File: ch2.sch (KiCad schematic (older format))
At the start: 0 parts

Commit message: ch1 and ch2 are complete
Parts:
- added C10, C9: 680p, symbol Device:C_Small
- added C11, C12: 47p, symbol Device:C_Small
- added C7, C8: 100p, symbol Device:C_Small
- added J2: CH2, symbol Connector:XLR3_Ground
- added Q201, Q211: BC856BDW1, Package_TO_SOT_SMD:SOT-363_SC-70-6, symbol Transistor_BJT:BC856BDW1
- added Q202, Q212: LS844, SOT95P280X145-6N, symbol LS844-SOT-23-6L-CT:LS844-SOT-23-6L-CT
- added Q203, Q213: BC846BDW1, Package_TO_SOT_SMD:SOT-363_SC-70-6, symbol Transistor_BJT:BC846BDW1
- added Q204, Q214: BC856, Package_TO_SOT_SMD:SOT-23, symbol Transistor_BJT:BC856
- added Q205, Q215: BCP53, Package_TO_SOT_SMD:SOT-223-3_TabPin2, symbol Transistor_BJT:BCP53
- added Q206, Q216: BC846, Package_TO_SOT_SMD:SOT-23, symbol Transistor_BJT:BC846
- added Q207, Q217: BCP56, Package_TO_SOT_SMD:SOT-223-3_TabPin2, symbol Transistor_BJT:BCP56
- added R28, R29, R33, R34, R35, R36, R43, R44, R45, R46, R53, R54: 100R, symbol Device:R_Small
- added R30: 2M2, symbol Device:R_Small
- added R31, R32: 47K, symbol Device:R_Small
- added R37, R38, R47, R48: 5K6, symbol Device:R_Small
- added R39, R40, R49, R50: 470R, symbol Device:R_Small
- added R41, R42: 330R, symbol Device:R_Small
- added R51, R52: 22R, symbol Device:R_Small
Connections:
- new net: J2.2, R28.2
- new net: J2.3, R29.2
- new net: R30.1, R31.1, R32.2
- new net: C11.2, Q201.1 (E1), Q202.2 (D1), Q204.1 (B), R39.2
- new net: Q202.3 (S1), R34.2
- new net: C11.1, Q202.4 (G2), Q205.2 (C), Q205.4 (C), Q207.2 (C), Q207.4 (C), R53.2
- new net: C9.1, Q201.2 (B1), Q201.4 (E2), Q201.5 (B2), Q202.5 (D2)
- new net: Q202.6 (S2), R44.2
- new net: C9.2, R39.1
- new net: Q201.6 (C1), R33.1
- new net: Q201.3 (C2), R43.1
- new net: Q203.6 (C1), R34.1, R44.1
- new net: Q203.2 (B1), Q203.3 (C2), R37.1
- new net: Q203.1 (E1), Q203.5 (B2), R41.2
- new net: Q204.2 (E), Q205.1 (B), R49.1
- new net: Q206.1 (B), Q207.3 (E), R51.2
- new net: Q206.3 (C), Q207.1 (B), R47.1
- new net: C12.2, Q211.1 (E1), Q212.2 (D1), Q214.1 (B), R40.2
- new net: Q212.3 (S1), R36.2
- new net: C12.1, Q212.4 (G2), Q215.2 (C), Q215.4 (C), Q217.2 (C), Q217.4 (C), R54.2
- new net: C10.1, Q211.2 (B1), Q211.4 (E2), Q211.5 (B2), Q212.5 (D2)
- new net: Q212.6 (S2), R46.2
- new net: C10.2, R40.1
- new net: Q211.6 (C1), R35.1
- new net: Q211.3 (C2), R45.1
- new net: Q213.6 (C1), R36.1, R46.1
- new net: Q213.2 (B1), Q213.3 (C2), R38.1
- new net: Q213.1 (E1), Q213.5 (B2), R42.2
- new net: Q214.2 (E), Q215.1 (B), R50.1
- new net: Q216.1 (B), Q217.3 (E), R52.2
- new net: Q216.3 (C), Q217.1 (B), R48.1
- new net +15V: Q205.3 (E), Q215.3 (E), R33.2, R35.2, R43.2, R45.2, R49.2, R50.2
- new net -15V: Q203.4 (E2), Q206.2 (E), Q213.4 (E2), Q216.2 (E), R41.1, R42.1, R51.1, R52.1
- new net CH2IN+: C7.1, Q202.1 (G1), R28.1, R31.2
- new net CH2IN-: C8.2, Q212.1 (G1), R29.1, R32.1
- new net CH2OUT+: R53.1
- new net CH2OUT-: R54.1
- new net GND: C7.2, C8.1, J2.1, J2.G, Q204.3 (C), Q214.3 (C), R30.2, R37.2, R38.2, R47.2, R48.2
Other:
- note added: "pg2xx"

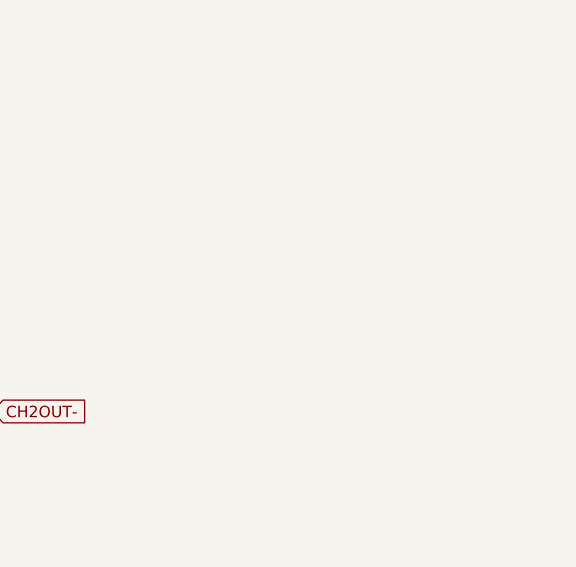
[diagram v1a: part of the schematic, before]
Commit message: assigned footprints
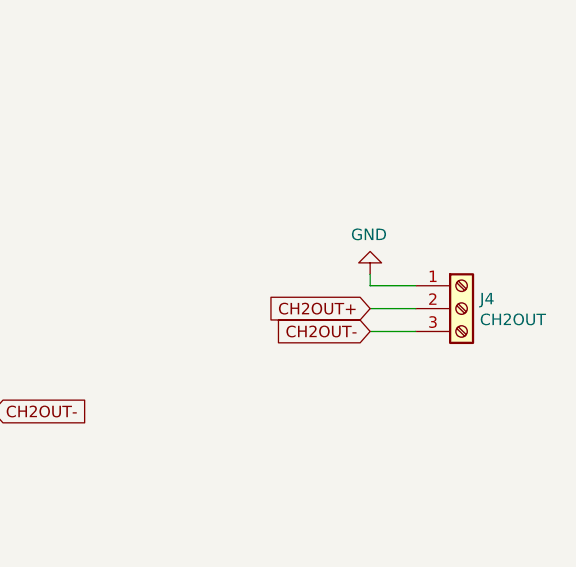
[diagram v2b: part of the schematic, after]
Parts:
- added J4: CH2OUT, TerminalBlock_Phoenix:TerminalBlock_Phoenix_PT-1,5-3-3.5-H_1x03_P3.50mm_Horizontal, symbol Connector:Screw_Terminal_01x03
- C10, C11, C12, C7, C8, C9: footprint (none) -> Capacitor_SMD:C_0805_2012Metric_Pad1.15x1.40mm_HandSolder
- J2: footprint (none) -> Connector_Audio:Jack_XLR_Neutrik_NC3FAAH2_Horizontal
- Q202, Q212: footprint SOT95P280X145-6N -> Package_TO_SOT_SMD:SOT-23-6
- R28, R29, R30, R31, R32, R33, R34, R35, R36, R37, R38, R39, R40, R41, R42, R43, R44, R45, R46, R47, R48, R49, R50, R51, R52, R53, R54: footprint (none) -> Resistor_SMD:R_0805_2012Metric_Pad1.15x1.40mm_HandSolder
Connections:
- net CH2OUT+: now also J4.2 (Pin_2)
- net CH2OUT-: now also J4.3 (Pin_3)
- net GND: now also J4.1 (Pin_1)

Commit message: pcb started
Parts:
- removed C10, C9: 680p, Capacitor_SMD:C_0805_2012Metric_Pad1.15x1.40mm_HandSolder, symbol Device:C_Small
- removed R39, R40: 470R, Resistor_SMD:R_0805_2012Metric_Pad1.15x1.40mm_HandSolder, symbol Device:R_Small
- removed R53, R54: 100R, Resistor_SMD:R_0805_2012Metric_Pad1.15x1.40mm_HandSolder, symbol Device:R_Small
- added C201, C202: 10u, Capacitor_THT:C_Radial_D5.0mm_H7.0mm_P2.00mm, symbol Device:C_Small
- C205: renamed from C11; value 47p -> 27p
- C206: renamed from C12; value 47p -> 27p
- renumbered C7 to C203, C8 to C204, J2 to J201, J4 to J202, R28 to R201, R29 to R202, R30 to R203, R31 to R204, R32 to R205, R33 to R206
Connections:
- net CH2OUT+: now also C205.1, Q202.4 (G2), Q205.2 (C), Q205.4 (C), Q207.2 (C), Q207.4 (C)
- net CH2OUT-: now also C206.1, Q212.4 (G2), Q215.2 (C), Q215.4 (C), Q217.2 (C), Q217.4 (C)
- net at J201.2: now also C201.2; no longer R201.2
- net at J201.3: now also C202.2; no longer R202.2
- net CH2+_FB: now reaches C205.2, Q201.1 (E1), Q202.2 (D1), Q204.1 (B)
- net CH2-_FB: now reaches C206.2, Q211.1 (E1), Q212.2 (D1), Q214.1 (B)
- new net: C201.1, R201.2
- new net: C202.1, R202.2
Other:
- moved on the sheet: C203, C204, C205, C206, J202, Q201A, Q201B, Q202, Q203A, Q203B, Q204, Q205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
